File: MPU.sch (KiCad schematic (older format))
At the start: 19 parts, among them U1 STM32MP151AAB3

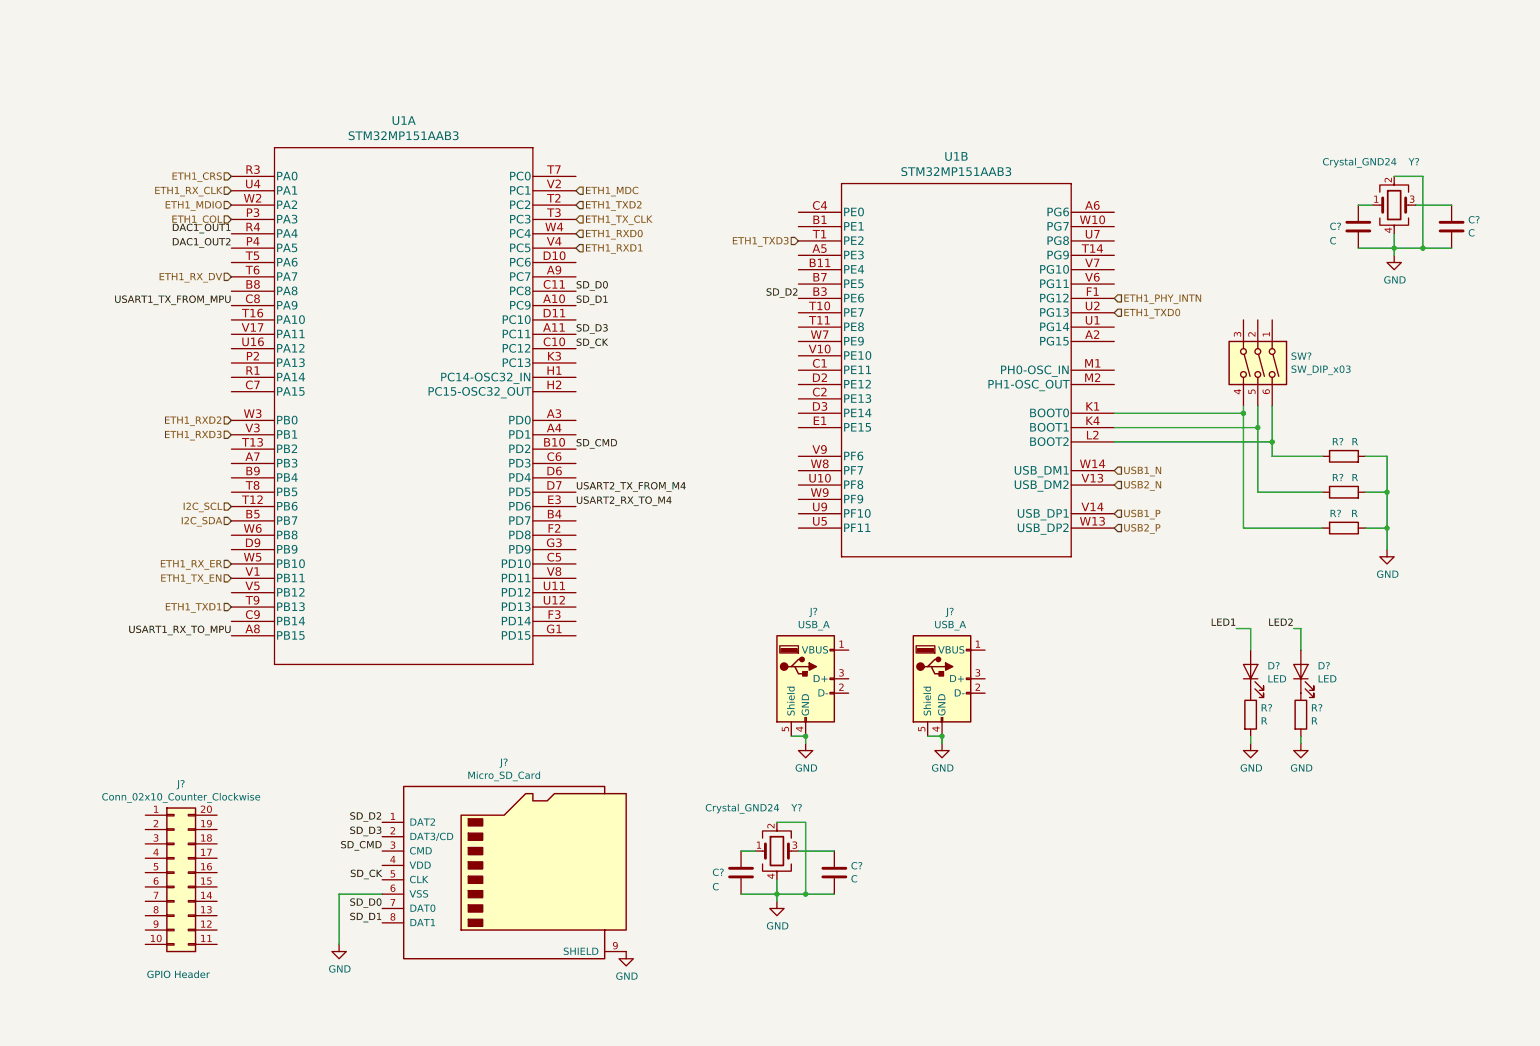
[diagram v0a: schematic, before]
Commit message: Add bulk labels for RAM and ethernet
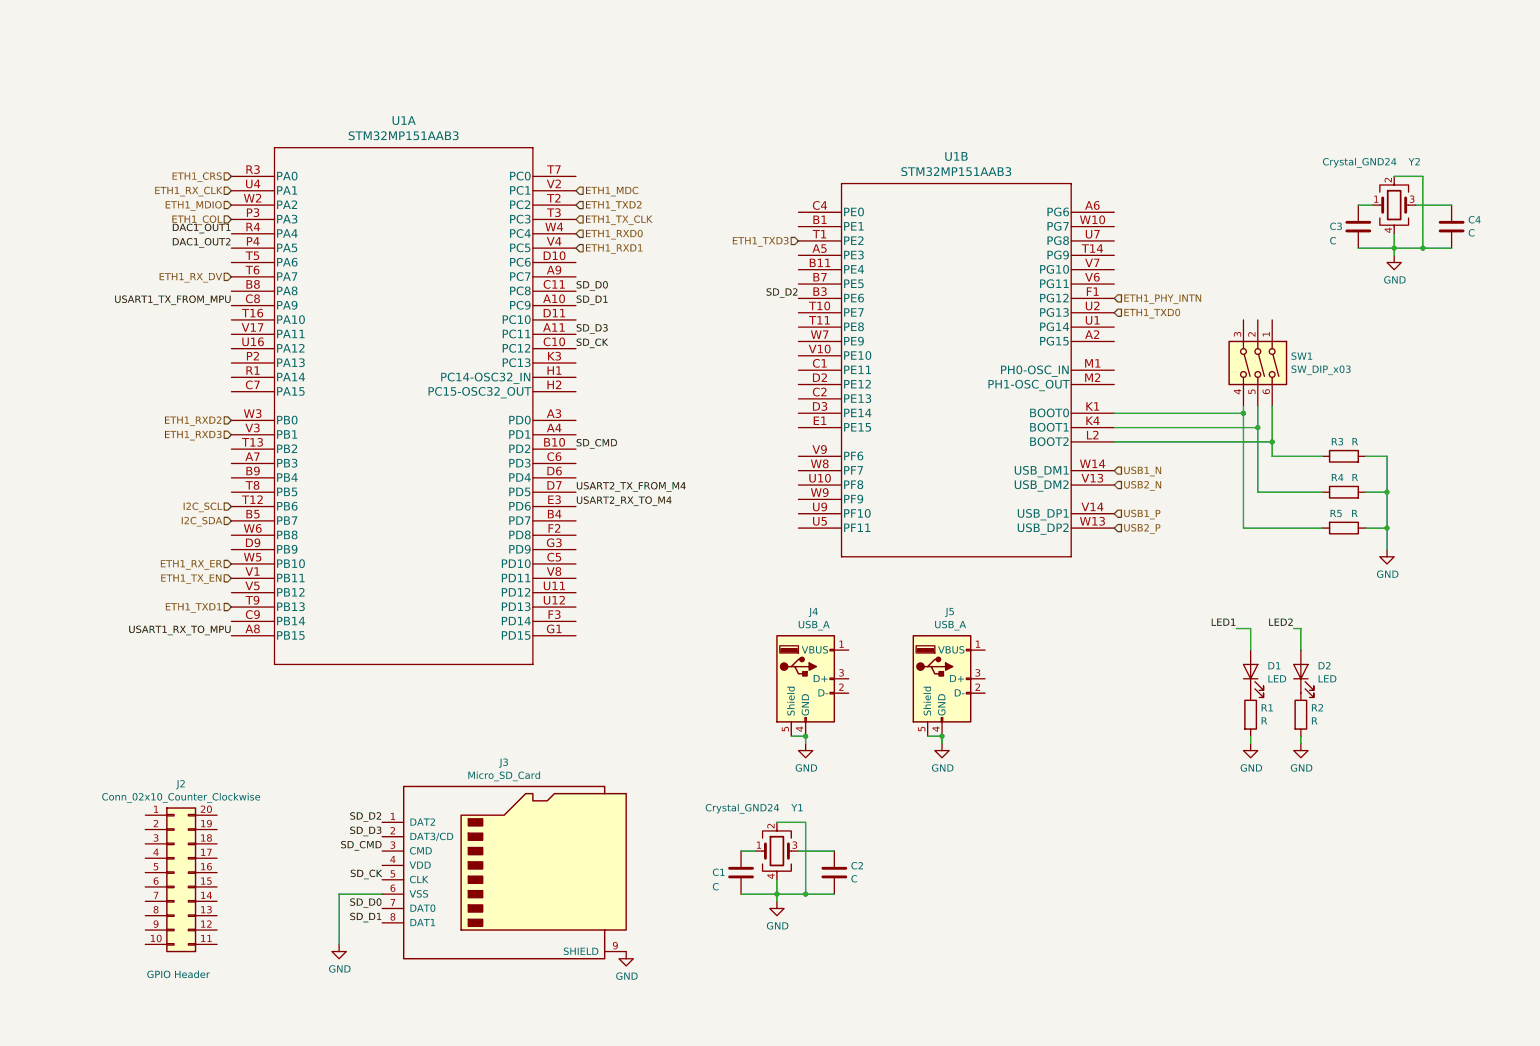
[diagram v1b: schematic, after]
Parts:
- C1, C2, C3, C4: renamed from C?; footprint (none) -> Capacitor_SMD:C_0603_1608Metric
- D1, D2: renamed from D?; footprint (none) -> LED_SMD:LED_0603_1608Metric
- J2: renamed from J?; footprint (none) -> Connector_IDC:IDC-Header_2x10_P2.54mm_Vertical
- J3: renamed from J?; footprint (none) -> Connector_Card:microSD_HC_Wuerth_693072010801
- J4, J5: renamed from J?; footprint (none) -> Connector_USB:USB_A_CNCTech_1001-011-01101_Horizontal
- R1, R2, R3, R4, R5: renamed from R?; footprint (none) -> Resistor_SMD:R_0603_1608Metric
- SW1: renamed from SW?; footprint (none) -> Button_Switch_SMD:SW_DIP_SPSTx03_Slide_Omron_A6S-310x_W8.9mm_P2.54mm
- Y1, Y2: renamed from Y?; footprint (none) -> Crystal:Crystal_SMD_2520-4Pin_2.5x2.0mm
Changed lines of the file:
@@
 ETH1_TXD0
 $Comp
-L Switch:SW_DIP_x03 SW?
+L Switch:SW_DIP_x03 SW1
 U 1 1 605563B9
 P 9100 3000
-F 0 "SW?" V 9054 3330 50  0000 L CNN
+F 0 "SW1" V 9054 3330 50  0000 L CNN
 F 1 "SW_DIP_x03" V 9145 3330 50  0000 L CNN
-F 2 "" H 9100 3000 50  0001 C CNN
+F 2 "Button_Switch_SMD:SW_DIP_SPSTx03_Slide_Omron_A6S-310x_W8.9mm_P2.54mm" H 9100 3000 50  0001 C CNN
 F 3 "~" H 9100 3000 50  0001 C CNN
 	1    9100 3000
@@
 	9300 3300 9300 3550
 $Comp
-L Device:R R?
+L Device:R R5
 U 1 1 6059A983
 P 9800 4150
-F 0 "R?" V 9700 4050 50  0000 L CNN
+F 0 "R5" V 9700 4050 50  0000 L CNN
 F 1 "R" V 9700 4200 50  0000 L CNN
-F 2 "" V 9730 4150 50  0001 C CNN
+F 2 "Resistor_SMD:R_0603_1608Metric" V 9730 4150 50  0001 C CNN
 F 3 "~" H 9800 4150 50  0001 C CNN
 	1    9800 4150
@@
 $EndComp
 $Comp
-L Device:R R?
+L Device:R R4
 U 1 1 6059B33B
 P 9800 3900
-F 0 "R?" V 9900 3900 50  0000 L CNN
+F 0 "R4" V 9900 3900 50  0000 L CNN
 F 1 "R" V 9900 3800 50  0000 L CNN
-F 2 "" V 9730 3900 50  0001 C CNN
+F 2 "Resistor_SMD:R_0603_1608Metric" V 9730 3900 50  0001 C CNN
 F 3 "~" H 9800 3900 50  0001 C CNN
 	1    9800 3900
@@
 $EndComp
 $Comp
-L Device:R R?
+L Device:R R3
 U 1 1 6059BCC5
 P 9800 3650
-F 0 "R?" V 9900 3650 50  0000 L CNN
+F 0 "R3" V 9900 3650 50  0000 L CNN
 F 1 "R" V 9900 3550 50  0000 L CNN
-F 2 "" V 9730 3650 50  0001 C CNN
+F 2 "Resistor_SMD:R_0603_1608Metric" V 9730 3650 50  0001 C CNN
 F 3 "~" H 9800 3650 50  0001 C CNN
 	1    9800 3650
@@
 Connection ~ 9300 3550
 $Comp
-L Device:Crystal_GND24 Y?
+L Device:Crystal_GND24 Y1
 U 1 1 6061525C
 P 5850 6400
-F 0 "Y?" H 5950 6700 50  0000 L CNN
+F 0 "Y1" H 5950 6700 50  0000 L CNN
 F 1 "Crystal_GND24" H 5350 6700 50  0000 L CNN
-F 2 "" H 5850 6400 50  0001 C CNN
+F 2 "Crystal:Crystal_SMD_2520-4Pin_2.5x2.0mm" H 5850 6400 50  0001 C CNN
 F 3 "~" H 5850 6400 50  0001 C CNN
 	1    5850 6400
@@
 P 9150 5450
 AR Path="/60172B24/60642C91" Ref="R?"  Part="1"
-AR Path="/601728C0/60642C91" Ref="R?"  Part="1"
-F 0 "R?" H 9220 5496 50  0000 L CNN
+AR Path="/601728C0/60642C91" Ref="R1"  Part="1"
+F 0 "R1" H 9220 5496 50  0000 L CNN
 F 1 "R" H 9220 5405 50  0000 L CNN
-F 2 "" V 9080 5450 50  0001 C CNN
+F 2 "Resistor_SMD:R_0603_1608Metric" V 9080 5450 50  0001 C CNN
 F 3 "~" H 9150 5450 50  0001 C CNN
 	1    9150 5450
@@
 P 9150 5150
 AR Path="/60172B24/60642C97" Ref="D?"  Part="1"
-AR Path="/601728C0/60642C97" Ref="D?"  Part="1"
-F 0 "D?" V 9189 5033 50  0000 R CNN
+AR Path="/601728C0/60642C97" Ref="D1"  Part="1"
+F 0 "D1" V 9189 5033 50  0000 R CNN
 F 1 "LED" V 9098 5033 50  0000 R CNN
-F 2 "" H 9150 5150 50  0001 C CNN
+F 2 "LED_SMD:LED_0603_1608Metric" H 9150 5150 50  0001 C CNN
 F 3 "~" H 9150 5150 50  0001 C CNN
 	1    9150 5150
@@
 P 9150 5650
 AR Path="/60172B24/60642C9E" Ref="#PWR?"  Part="1"
-AR Path="/601728C0/60642C9E" Ref="#PWR?"  Part="1"
-F 0 "#PWR?" H 9150 5400 50  0001 C CNN
+AR Path="/601728C0/60642C9E" Ref="#PWR06"  Part="1"
+F 0 "#PWR06" H 9150 5400 50  0001 C CNN
 F 1 "GND" H 9155 5477 50  0000 C CNN
 F 2 "" H 9150 5650 50  0001 C CNN
@@
 P 9500 5450
 AR Path="/60172B24/60644ED5" Ref="R?"  Part="1"
-AR Path="/601728C0/60644ED5" Ref="R?"  Part="1"
-F 0 "R?" H 9570 5496 50  0000 L CNN
+AR Path="/601728C0/60644ED5" Ref="R2"  Part="1"
+F 0 "R2" H 9570 5496 50  0000 L CNN
 F 1 "R" H 9570 5405 50  0000 L CNN
-F 2 "" V 9430 5450 50  0001 C CNN
+F 2 "Resistor_SMD:R_0603_1608Metric" V 9430 5450 50  0001 C CNN
 F 3 "~" H 9500 5450 50  0001 C CNN
 	1    9500 5450
@@
 P 9500 5150
 AR Path="/60172B24/60644EDB" Ref="D?"  Part="1"
-AR Path="/601728C0/60644EDB" Ref="D?"  Part="1"
-F 0 "D?" V 9539 5033 50  0000 R CNN
+AR Path="/601728C0/60644EDB" Ref="D2"  Part="1"
+F 0 "D2" V 9539 5033 50  0000 R CNN
 F 1 "LED" V 9448 5033 50  0000 R CNN
-F 2 "" H 9500 5150 50  0001 C CNN
+F 2 "LED_SMD:LED_0603_1608Metric" H 9500 5150 50  0001 C CNN
 F 3 "~" H 9500 5150 50  0001 C CNN
 	1    9500 5150
@@
 P 9500 5650
 AR Path="/60172B24/60644EE2" Ref="#PWR?"  Part="1"
-AR Path="/601728C0/60644EE2" Ref="#PWR?"  Part="1"
-F 0 "#PWR?" H 9500 5400 50  0001 C CNN
+AR Path="/601728C0/60644EE2" Ref="#PWR07"  Part="1"
+F 0 "#PWR07" H 9500 5400 50  0001 C CNN
 F 1 "GND" H 9505 5477 50  0000 C CNN
 F 2 "" H 9500 5650 50  0001 C CNN
@@
 USB2_P
 $Comp
-L Connector:Micro_SD_Card J?
+L Connector:Micro_SD_Card J3
 U 1 1 60681963
 P 4000 6500
-F 0 "J?" H 3950 7217 50  0000 C CNN
+F 0 "J3" H 3950 7217 50  0000 C CNN
 F 1 "Micro_SD_Card" H 3950 7126 50  0000 C CNN
-F 2 "" H 5150 6800 50  0001 C CNN
+F 2 "Connector_Card:microSD_HC_Wuerth_693072010801" H 5150 6800 50  0001 C CNN
 F 3 "http://katalog.we-online.de/em/datasheet/693072010801.pdf" H 4000 6500 50  0001 C CNN
 	1    4000 6500
@@
 $EndComp
 $Comp
-L power:GND #PWR?
+L power:GND #PWR02
 U 1 1 6068FAB3
 P 4800 7100
-F 0 "#PWR?" H 4800 6850 50  0001 C CNN
+F 0 "#PWR02" H 4800 6850 50  0001 C CNN
 F 1 "GND" H 4805 6927 50  0000 C CNN
 F 2 "" H 4800 7100 50  0001 C CNN
@@
 SD_CK
 $Comp
-L power:GND #PWR?
+L power:GND #PWR01
 U 1 1 606B1775
 P 2800 7050
-F 0 "#PWR?" H 2800 6800 50  0001 C CNN
+F 0 "#PWR01" H 2800 6800 50  0001 C CNN
 F 1 "GND" H 2805 6877 50  0000 C CNN
 F 2 "" H 2800 7050 50  0001 C CNN
@@
 I2C_SDA
 $Comp
-L power:GND #PWR?
+L power:GND #PWR08
 U 1 1 6107D211
 P 10100 4300
-F 0 "#PWR?" H 10100 4050 50  0001 C CNN
+F 0 "#PWR08" H 10100 4050 50  0001 C CNN
 F 1 "GND" H 10105 4127 50  0000 C CNN
 F 2 "" H 10100 4300 50  0001 C CNN
@@
 Connection ~ 10100 3900
 $Comp
-L Connector_Generic:Conn_02x10_Counter_Clockwise J?
+L Connector_Generic:Conn_02x10_Counter_Clockwise J2
 U 1 1 6112FDF3
 P 1650 6550
-F 0 "J?" H 1700 7167 50  0000 C CNN
+F 0 "J2" H 1700 7167 50  0000 C CNN
 F 1 "Conn_02x10_Counter_Clockwise" H 1700 7076 50  0000 C CNN
-F 2 "" H 1650 6550 50  0001 C CNN
+F 2 "Connector_IDC:IDC-Header_2x10_P2.54mm_Vertical" H 1650 6550 50  0001 C CNN
 F 3 "~" H 1650 6550 50  0001 C CNN
 	1    1650 6550
@@
 	5850 6700 5850 6600
 $Comp
-L power:GND #PWR?
+L power:GND #PWR03
 U 1 1 61194FE7
 P 5850 6750
-F 0 "#PWR?" H 5850 6500 50  0001 C CNN
+F 0 "#PWR03" H 5850 6500 50  0001 C CNN
 F 1 "GND" H 5855 6577 50  0000 C CNN
 F 2 "" H 5850 6750 50  0001 C CNN
@@
 Connection ~ 5850 6700
 $Comp
-L Device:C C?
+L Device:C C2
 U 1 1 61197B94
 P 6250 6550
-F 0 "C?" H 6365 6596 50  0000 L CNN
+F 0 "C2" H 6365 6596 50  0000 L CNN
 F 1 "C" H 6365 6505 50  0000 L CNN
-F 2 "" H 6288 6400 50  0001 C CNN
+F 2 "Capacitor_SMD:C_0603_1608Metric" H 6288 6400 50  0001 C CNN
 F 3 "~" H 6250 6550 50  0001 C CNN
 	1    6250 6550
@@
 	5600 6700 5850 6700
 $Comp
-L Device:C C?
+L Device:C C1
 U 1 1 6119821B
 P 5600 6550
-F 0 "C?" H 5400 6550 50  0000 L CNN
+F 0 "C1" H 5400 6550 50  0000 L CNN
 F 1 "C" H 5400 6450 50  0000 L CNN
-F 2 "" H 5638 6400 50  0001 C CNN
+F 2 "Capacitor_SMD:C_0603_1608Metric" H 5638 6400 50  0001 C CNN
 F 3 "~" H 5600 6550 50  0001 C CNN
 	1    5600 6550
@@
 $EndComp
 $Comp
-L Device:Crystal_GND24 Y?
+L Device:Crystal_GND24 Y2
 U 1 1 611BD934
 P 10150 1900
-F 0 "Y?" H 10250 2200 50  0000 L CNN
+F 0 "Y2" H 10250 2200 50  0000 L CNN
 F 1 "Crystal_GND24" H 9650 2200 50  0000 L CNN
-F 2 "" H 10150 1900 50  0001 C CNN
+F 2 "Crystal:Crystal_SMD_2520-4Pin_2.5x2.0mm" H 10150 1900 50  0001 C CNN
 F 3 "~" H 10150 1900 50  0001 C CNN
 	1    10150 1900
@@
 	10150 2200 10150 2100
 $Comp
-L power:GND #PWR?
+L power:GND #PWR09
 U 1 1 611BD93E
 P 10150 2250
-F 0 "#PWR?" H 10150 2000 50  0001 C CNN
+F 0 "#PWR09" H 10150 2000 50  0001 C CNN
 F 1 "GND" H 10155 2077 50  0000 C CNN
 F 2 "" H 10150 2250 50  0001 C CNN
@@
 Connection ~ 10150 2200
 $Comp
-L Device:C C?
+L Device:C C4
 U 1 1 611BD946
 P 10550 2050
-F 0 "C?" H 10665 2096 50  0000 L CNN
+F 0 "C4" H 10665 2096 50  0000 L CNN
 F 1 "C" H 10665 2005 50  0000 L CNN
-F 2 "" H 10588 1900 50  0001 C CNN
+F 2 "Capacitor_SMD:C_0603_1608Metric" H 10588 1900 50  0001 C CNN
 F 3 "~" H 10550 2050 50  0001 C CNN
 	1    10550 2050
@@
 	9900 2200 10150 2200
 $Comp
-L Device:C C?
+L Device:C C3
 U 1 1 611BD951
 P 9900 2050
-F 0 "C?" H 9700 2050 50  0000 L CNN
+F 0 "C3" H 9700 2050 50  0000 L CNN
 F 1 "C" H 9700 1950 50  0000 L CNN
-F 2 "" H 9938 1900 50  0001 C CNN
+F 2 "Capacitor_SMD:C_0603_1608Metric" H 9938 1900 50  0001 C CNN
 F 3 "~" H 9900 2050 50  0001 C CNN
 	1    9900 2050
@@
 	9500 4850 9500 5000
 $Comp
-L Connector:USB_A J?
+L Connector:USB_A J4
 U 1 1 612273A9
 P 6050 5200
-F 0 "J?" H 6107 5667 50  0000 C CNN
+F 0 "J4" H 6107 5667 50  0000 C CNN
 F 1 "USB_A" H 6107 5576 50  0000 C CNN
-F 2 "" H 6200 5150 50  0001 C CNN
+F 2 "Connector_USB:USB_A_CNCTech_1001-011-01101_Horizontal" H 6200 5150 50  0001 C CNN
 F 3 " ~" H 6200 5150 50  0001 C CNN
 	1    6050 5200
@@
 $EndComp
 $Comp
-L Connector:USB_A J?
+L Connector:USB_A J5
 U 1 1 612403B4
 P 7000 5200
-F 0 "J?" H 7057 5667 50  0000 C CNN
+F 0 "J5" H 7057 5667 50  0000 C CNN
 F 1 "USB_A" H 7057 5576 50  0000 C CNN
-F 2 "" H 7150 5150 50  0001 C CNN
+F 2 "Connector_USB:USB_A_CNCTech_1001-011-01101_Horizontal" H 7150 5150 50  0001 C CNN
 F 3 " ~" H 7150 5150 50  0001 C CNN
 	1    7000 5200
@@
 	6900 5600 7000 5600
 $Comp
-L power:GND #PWR?
+L power:GND #PWR04
 U 1 1 6125217E
 P 6050 5650
-F 0 "#PWR?" H 6050 5400 50  0001 C CNN
+F 0 "#PWR04" H 6050 5400 50  0001 C CNN
 F 1 "GND" H 6055 5477 50  0000 C CNN
 F 2 "" H 6050 5650 50  0001 C CNN
@@
 Connection ~ 6050 5600
 $Comp
-L power:GND #PWR?
+L power:GND #PWR05
 U 1 1 61254080
 P 7000 5650
-F 0 "#PWR?" H 7000 5400 50  0001 C CNN
+F 0 "#PWR05" H 7000 5400 50  0001 C CNN
 F 1 "GND" H 7005 5477 50  0000 C CNN
 F 2 "" H 7000 5650 50  0001 C CNN
